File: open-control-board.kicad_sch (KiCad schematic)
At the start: 123 parts, among them CN1 Service boiler fill sensor, CN10 LCC Port, CN2 Water tank level switch, CN3 NTC Service Boiler, CN4 NTC Brew Boiler, CN5 Service boiler relay, CN6 Conn_02x04_Counter_Clockwise, CN7 Brew Switch, CN8 12V Separate Supply, CN9 Brew boiler relay, J1 USB_B_Micro, J10 Conn_01x04_Pin, J11 Conn_01x04_Pin, J12 Conn_02x06_Odd_Even, J13 Conn_02x05_Odd_Even, J14 Conn_02x04_Odd_Even, J15 Conn_02x05_Odd_Even, J16 USB_B_Micro, J18 Conn_01x03_Pin, J5 BM04B-SRSS-TB(LF)(SN), Q1 AO3401A, Q11 DMN63D8LDW, Q2 AO3401A, Q3 FDC6306P, Q4 DMN63D8LDW, Q5 FDC6306P, Q6 DMN63D8LDW, SW1 SW_Push, SW2 SW_Push, SW3 SW_Push, SW4 SW_Push, U10 FDC1004, U15 STPIC6C595TTR, U16 STPIC6C595TTR, U2 RP2040, U3 ESP32-S3-WROOM-1, U4 W25Q16JVUXIQ, U6 TPS82130, U7 TXB0108PWR, U8 ADS1115IDGS, Y1 XYDBPCNANF-12MHZ

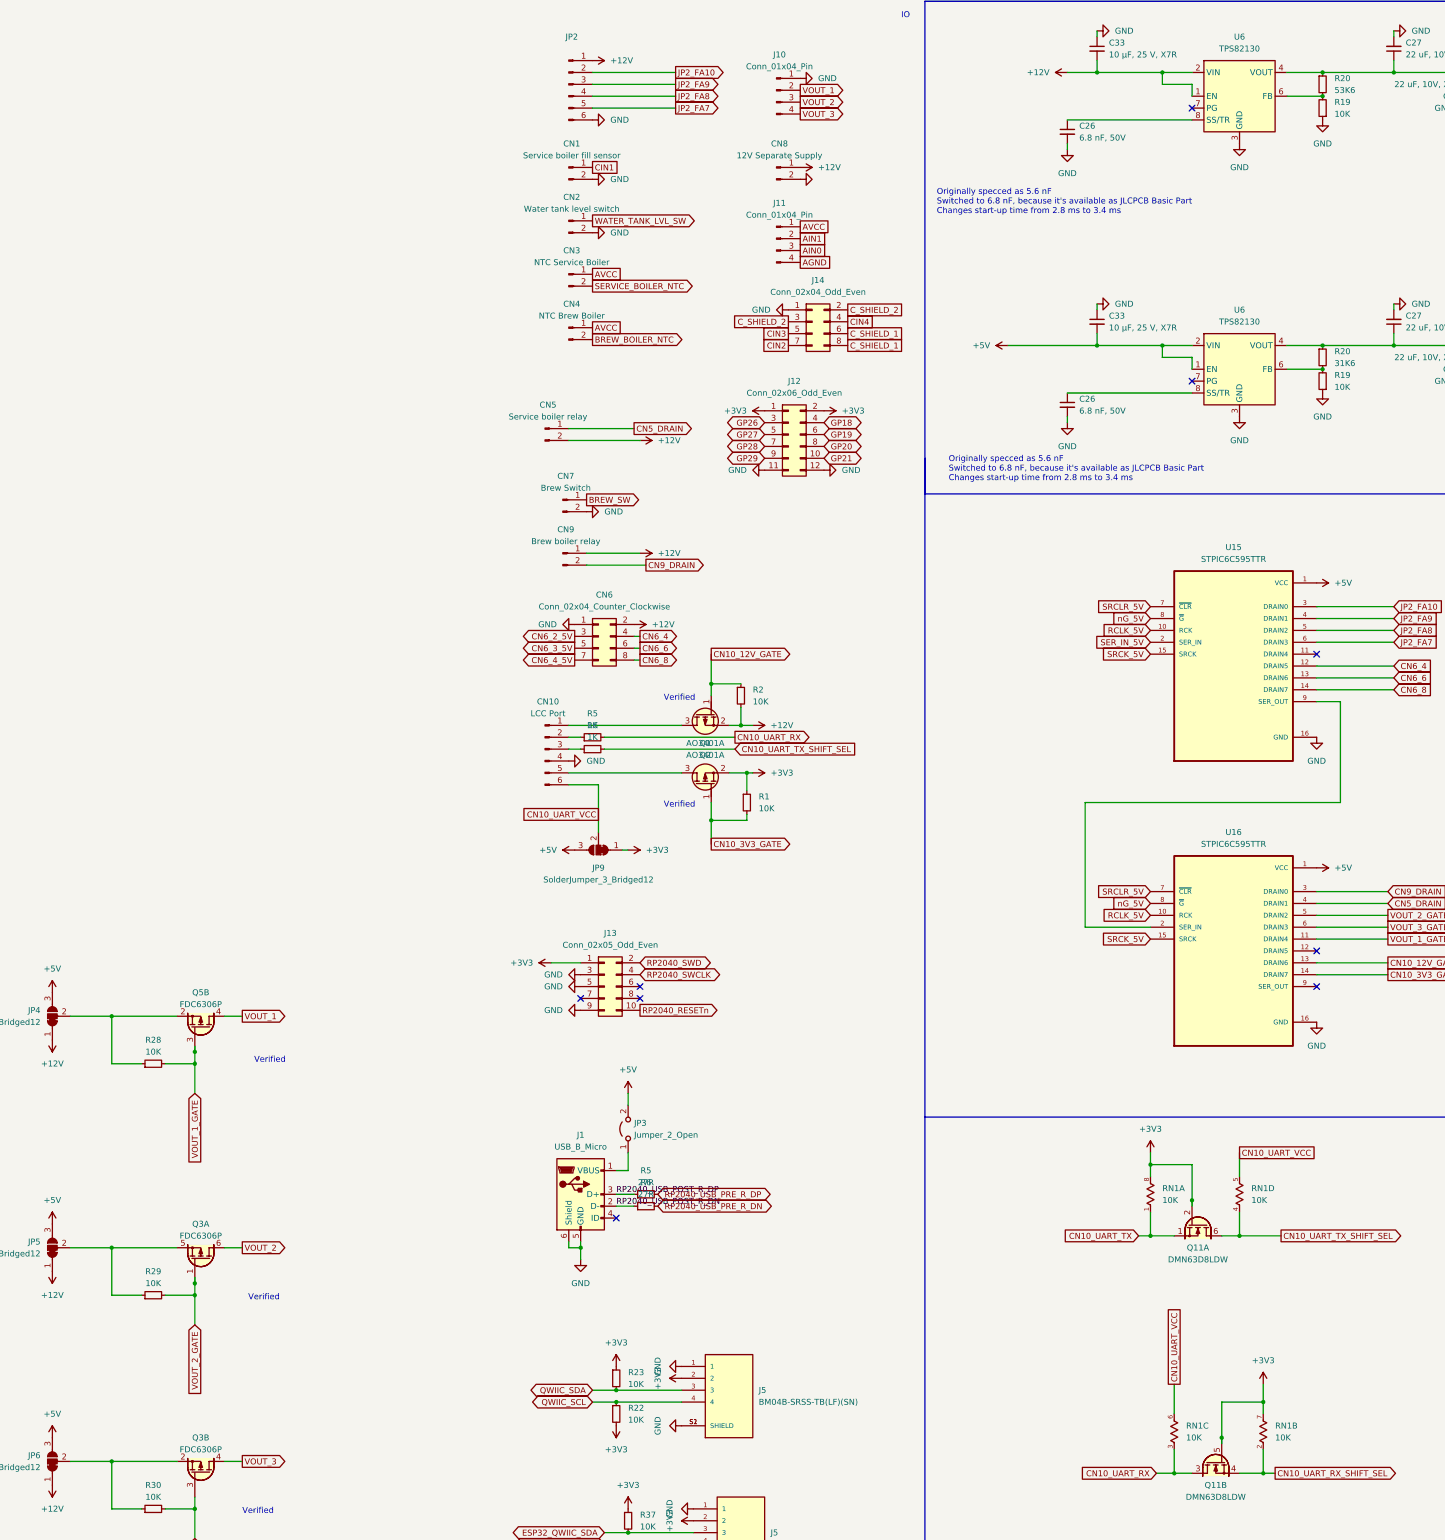
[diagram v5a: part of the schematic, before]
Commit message: Cheaper resistors
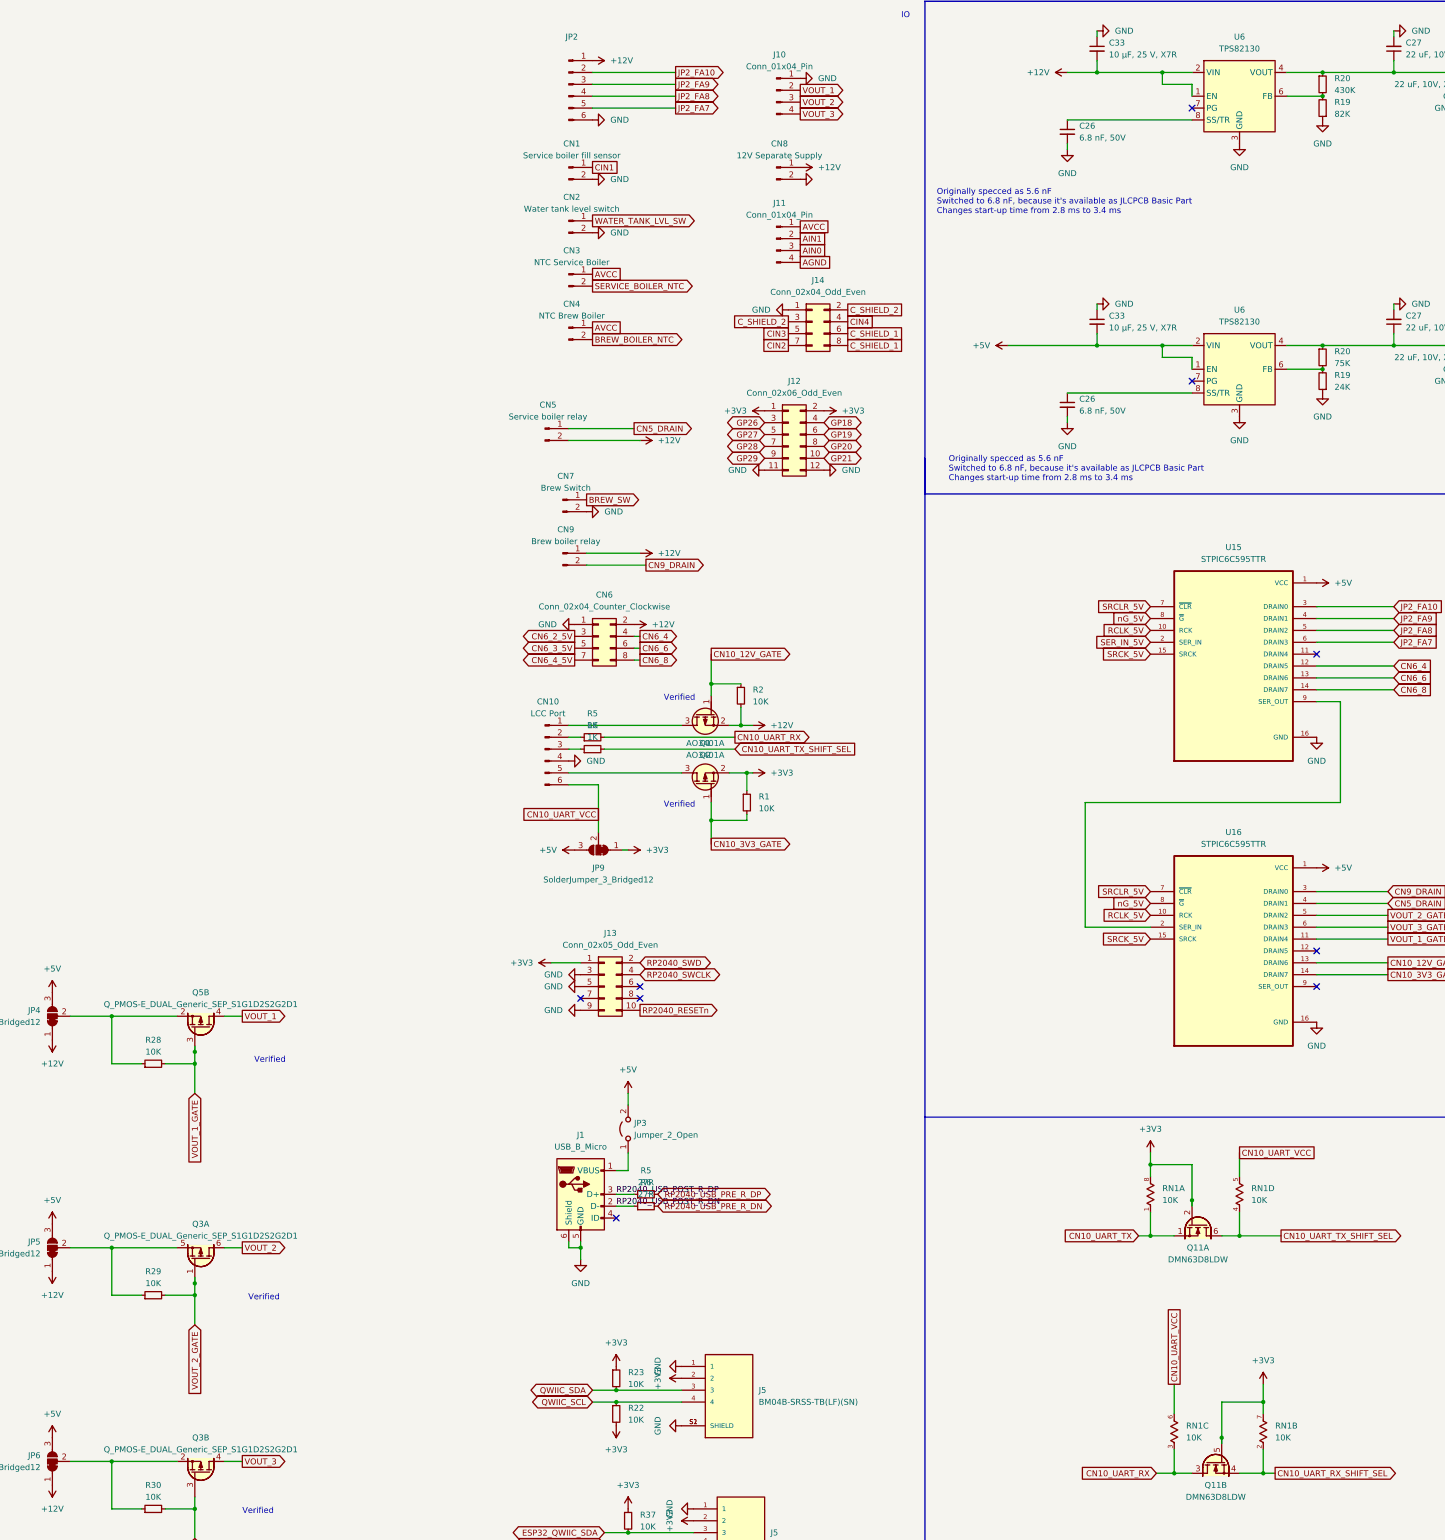
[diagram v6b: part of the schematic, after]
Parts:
- Q3, Q5: value FDC6306P -> Q_PMOS-E_DUAL_Generic_SEP_S1G1D2S2G2D1; LCSC C558119 -> C124461
- R19: value 10K -> 24K; footprint Resistor_SMD:R_0402_1005Metric -> Resistor_SMD:R_0603_1608Metric; LCSC C25744 -> C23352
- R19: value 10K -> 82K; footprint Resistor_SMD:R_0402_1005Metric -> Resistor_SMD:R_0603_1608Metric; LCSC C25744 -> C23254
- R20: value 53K6 -> 430K; footprint Resistor_SMD:R_0402_1005Metric -> Resistor_SMD:R_0603_1608Metric; LCSC C53398 -> C25969
- R20: value 31K6 -> 75K; footprint Resistor_SMD:R_0402_1005Metric -> Resistor_SMD:R_0603_1608Metric; LCSC C11463 -> C23242
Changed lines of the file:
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@@
       (effects (font (size 1.27 1.27)) (justify right))
     )
-    (property "Value" "10K" (at 191.77 95.25 0)
+    (property "Value" "24K" (at 191.77 95.25 0)
       (effects (font (size 1.27 1.27)) (justify right))
     )
-    (property "Footprint" "Resistor_SMD:R_0402_1005Metric" (at 189.23 93.98 0)
+    (property "Footprint" "Resistor_SMD:R_0603_1608Metric" (at 189.23 93.98 0)
       (effects (font (size 1.27 1.27)) hide)
     )
@@
       (effects (font (size 1.27 1.27)) hide)
     )
-    (property "LCSC" "C25744" (at 189.23 93.98 0)
+    (property "LCSC" "C23352" (at 189.23 93.98 0)
       (effects (font (size 1.27 1.27)) hide)
     )
@@
       (effects (font (size 1.27 1.27)) (justify left))
     )
-    (property "Value" "53K6" (at 191.77 31.75 0)
+    (property "Value" "430K" (at 191.77 31.75 0)
       (effects (font (size 1.27 1.27)) (justify left))
     )
-    (property "Footprint" "Resistor_SMD:R_0402_1005Metric" (at 189.23 30.48 0)
+    (property "Footprint" "Resistor_SMD:R_0603_1608Metric" (at 189.23 30.48 0)
       (effects (font (size 1.27 1.27)) hide)
     )
@@
       (effects (font (size 1.27 1.27)) hide)
     )
-    (property "LCSC" "C53398" (at 189.23 30.48 0)
+    (property "LCSC" "C25969" (at 189.23 30.48 0)
       (effects (font (size 1.27 1.27)) hide)
     )
@@
       (effects (font (size 1.27 1.27)))
     )
-    (property "Value" "FDC6306P" (at -50.8 276.86 90)
+    (property "Value" "Q_PMOS-E_DUAL_Generic_SEP_S1G1D2S2G2D1" (at -50.8 276.86 90)
       (effects (font (size 1.27 1.27)))
     )
@@
       (effects (font (size 1.27 1.27)) hide)
     )
-    (property "LCSC" "C558119" (at -50.8 280.67 0)
+    (property "LCSC" "C124461" (at -50.8 280.67 0)
       (effects (font (size 1.27 1.27)) hide)
     )
@@
       (effects (font (size 1.27 1.27)))
     )
-    (property "Value" "FDC6306P" (at -50.8 227.33 90)
+    (property "Value" "Q_PMOS-E_DUAL_Generic_SEP_S1G1D2S2G2D1" (at -50.8 227.33 90)
       (effects (font (size 1.27 1.27)))
     )
@@
       (effects (font (size 1.27 1.27)) hide)
     )
-    (property "LCSC" "C558119" (at -50.8 231.14 0)
+    (property "LCSC" "C124461" (at -50.8 231.14 0)
       (effects (font (size 1.27 1.27)) hide)
     )
@@
       (effects (font (size 1.27 1.27)))
     )
-    (property "Value" "FDC6306P" (at -50.8 322.58 90)
+    (property "Value" "Q_PMOS-E_DUAL_Generic_SEP_S1G1D2S2G2D1" (at -50.8 322.58 90)
       (effects (font (size 1.27 1.27)))
     )
@@
       (effects (font (size 1.27 1.27)) hide)
     )
-    (property "LCSC" "C558119" (at -50.8 326.39 0)
+    (property "LCSC" "C124461" (at -50.8 326.39 0)
       (effects (font (size 1.27 1.27)) hide)
     )
@@
       (effects (font (size 1.27 1.27)) (justify right))
     )
-    (property "Value" "10K" (at 191.77 36.83 0)
+    (property "Value" "82K" (at 191.77 36.83 0)
       (effects (font (size 1.27 1.27)) (justify right))
     )
-    (property "Footprint" "Resistor_SMD:R_0402_1005Metric" (at 189.23 35.56 0)
+    (property "Footprint" "Resistor_SMD:R_0603_1608Metric" (at 189.23 35.56 0)
       (effects (font (size 1.27 1.27)) hide)
     )
@@
       (effects (font (size 1.27 1.27)) hide)
     )
-    (property "LCSC" "C25744" (at 189.23 35.56 0)
+    (property "LCSC" "C23254" (at 189.23 35.56 0)
       (effects (font (size 1.27 1.27)) hide)
     )
@@
       (effects (font (size 1.27 1.27)) (justify left))
     )
-    (property "Value" "31K6" (at 191.77 90.17 0)
+    (property "Value" "75K" (at 191.77 90.17 0)
       (effects (font (size 1.27 1.27)) (justify left))
     )
-    (property "Footprint" "Resistor_SMD:R_0402_1005Metric" (at 189.23 88.9 0)
+    (property "Footprint" "Resistor_SMD:R_0603_1608Metric" (at 189.23 88.9 0)
       (effects (font (size 1.27 1.27)) hide)
     )
@@
       (effects (font (size 1.27 1.27)) hide)
     )
-    (property "LCSC" "C11463" (at 189.23 88.9 0)
+    (property "LCSC" "C23242" (at 189.23 88.9 0)
       (effects (font (size 1.27 1.27)) hide)
     )

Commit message: Split HV board into separate project
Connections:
- net +3V3: now also JP13.3 (B); no longer JP13.1 (A)
- net +5V: now also JP13.1 (A); no longer JP13.3 (B)
- net GP15: now also U3.31 (GPIO38/FSPIWP/SUBSPIWP)
- no-connect marks 23 -> 22
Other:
- removed sheet Control Board HV Side
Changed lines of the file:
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@@
   (no_connect (at 561.34 184.15))
   (no_connect (at 400.05 368.3))
-  (no_connect (at 615.95 110.49))
   (no_connect (at 403.86 360.68))
   (no_connect (at 43.18 226.06))
@@
     )
   )
-  (global_label "CN6_3_3V3" (shape output) (at 170.18 400.05 270) (fields_autoplaced)
+  (global_label "CN6_3_3V3" (shape bidirectional) (at 170.18 400.05 270) (fields_autoplaced)
     (effects (font (size 1.27 1.27)) (justify right))
-    (property "Intersheetrefs" "${INTERSHEET_REFS}" (at 170.18 413.4975 90)
+    (property "Intersheetrefs" "${INTERSHEET_REFS}" (at 170.18 414.6088 90)
       (effects (font (size 1.27 1.27)) (justify right) hide)
     )
@@
     )
   )
-  (global_label "CN6_3_5V" (shape input) (at 170.18 373.38 90) (fields_autoplaced)
+  (global_label "CN6_3_5V" (shape bidirectional) (at 170.18 373.38 90) (fields_autoplaced)
     (effects (font (size 1.27 1.27)) (justify left))
-    (property "Intersheetrefs" "${INTERSHEET_REFS}" (at 170.18 361.142 90)
+    (property "Intersheetrefs" "${INTERSHEET_REFS}" (at 170.18 360.0307 90)
       (effects (font (size 1.27 1.27)) (justify left) hide)
     )
@@
     )
   )
-  (global_label "CN6_2_5V" (shape input) (at 172.72 373.38 90) (fields_autoplaced)
+  (global_label "CN6_2_5V" (shape bidirectional) (at 172.72 373.38 90) (fields_autoplaced)
     (effects (font (size 1.27 1.27)) (justify left))
-    (property "Intersheetrefs" "${INTERSHEET_REFS}" (at 172.72 361.142 90)
+    (property "Intersheetrefs" "${INTERSHEET_REFS}" (at 172.72 360.0307 90)
       (effects (font (size 1.27 1.27)) (justify left) hide)
     )
@@
     )
   )
-  (global_label "CN6_4_5V" (shape input) (at 167.64 373.38 90) (fields_autoplaced)
+  (global_label "CN6_4_5V" (shape bidirectional) (at 167.64 373.38 90) (fields_autoplaced)
     (effects (font (size 1.27 1.27)) (justify left))
-    (property "Intersheetrefs" "${INTERSHEET_REFS}" (at 167.64 361.142 90)
+    (property "Intersheetrefs" "${INTERSHEET_REFS}" (at 167.64 360.0307 90)
       (effects (font (size 1.27 1.27)) (justify left) hide)
     )
@@
     )
   )
+  (global_label "GP15" (shape bidirectional) (at 615.95 110.49 0) (fields_autoplaced)
+    (effects (font (size 1.27 1.27)) (justify left))
+    (property "Intersheetrefs" "${INTERSHEET_REFS}" (at 625.0055 110.49 0)
+      (effects (font (size 1.27 1.27)) (justify left) hide)
+    )
+  )
   (global_label "SRCLR_5V" (shape input) (at 152.4 142.24 180) (fields_autoplaced)
     (effects (font (size 1.27 1.27)) (justify right))
@@
     )
   )
-  (global_label "CN6_2_3V3" (shape output) (at 167.64 400.05 270) (fields_autoplaced)
+  (global_label "CN6_2_3V3" (shape bidirectional) (at 167.64 400.05 270) (fields_autoplaced)
     (effects (font (size 1.27 1.27)) (justify right))
-    (property "Intersheetrefs" "${INTERSHEET_REFS}" (at 167.64 413.4975 90)
+    (property "Intersheetrefs" "${INTERSHEET_REFS}" (at 167.64 414.6088 90)
       (effects (font (size 1.27 1.27)) (justify right) hide)
     )
@@
     )
   )
-  (global_label "CN6_4_3V3" (shape output) (at 172.72 400.05 270) (fields_autoplaced)
+  (global_label "CN6_4_3V3" (shape bidirectional) (at 172.72 400.05 270) (fields_autoplaced)
     (effects (font (size 1.27 1.27)) (justify right))
-    (property "Intersheetrefs" "${INTERSHEET_REFS}" (at 172.72 413.4975 90)
+    (property "Intersheetrefs" "${INTERSHEET_REFS}" (at 172.72 414.6088 90)
       (effects (font (size 1.27 1.27)) (justify right) hide)
     )
@@
     )
   )
-  (netclass_flag "" (length 2.54) (shape round) (at 189.23 220.98 0) (fields_autoplaced)
-    (effects (font (size 1.27 1.27)) (justify left bottom))
-    (property "Netclass" "12V_Thin" (at 189.9285 218.44 0)
-      (effects (font (size 1.27 1.27) italic) (justify left))
-    )
-  )
   (netclass_flag "" (length 2.54) (shape round) (at -52.07 339.09 270) (fields_autoplaced)
     (effects (font (size 1.27 1.27)) (justify right bottom))
@@
     )
   )
-  (symbol (lib_id "Jumper:SolderJumper_3_Bridged12") (at 307.34 254 0) (unit 1)
+  (symbol (lib_id "Jumper:SolderJumper_3_Bridged12") (at 307.34 254 0) (mirror y) (unit 1)
     (in_bom yes) (on_board yes) (dnp no)
-    (property "Reference" "JP13" (at 304.8 251.46 0)
+    (property "Reference" "JP13" (at 309.88 251.46 0)
       (effects (font (size 1.27 1.27)) (justify left))
     )
-    (property "Value" "SolderJumper_3_Bridged12" (at 275.59 248.92 0)
+    (property "Value" "SolderJumper_3_Bridged12" (at 339.09 248.92 0)
       (effects (font (size 1.27 1.27)) (justify left) hide)
     )
@@
       )
     )
-  )
-  (sheet (at 844.55 41.91) (size 209.55 171.45) (fields_autoplaced)
-    (stroke (width 0.1524) (type solid))
-    (fill (color 0 0 0 0.0000))
-    (property "Sheetname" "Control Board HV Side" (at 844.55 41.1984 0)
-      (effects (font (size 1.27 1.27)) (justify left bottom))
-    )
-    (property "Sheetfile" "untitled.kicad_sch" (at 844.55 213.9446 0)
-      (effects (font (size 1.27 1.27)) (justify left top))
-    )
-    (instances
-      (project "open-control-board"
-        (path "/c7c8c763-88fa-419b-8f4a-ebade330cc39" (page "2"))
-      )
-    )
